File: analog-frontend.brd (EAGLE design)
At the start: 26.7 x 25.1 mm, 2 parts

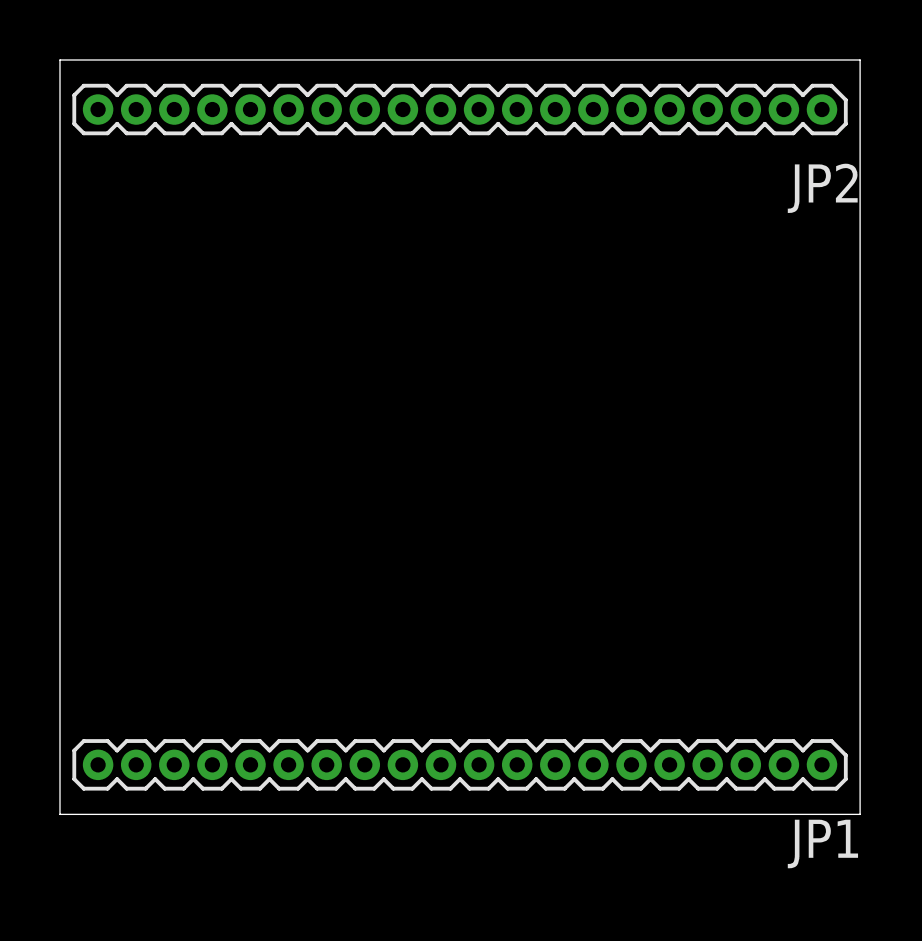
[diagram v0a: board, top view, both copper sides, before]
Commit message: added analog mux
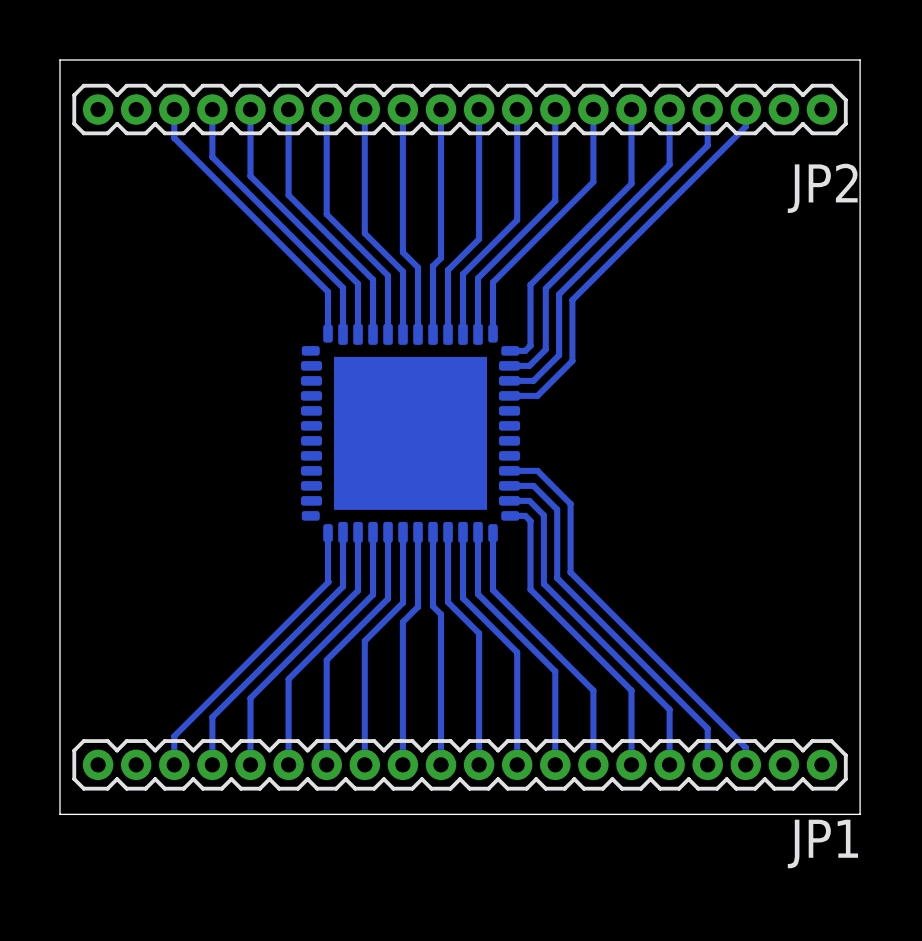
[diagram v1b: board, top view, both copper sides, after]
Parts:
- added IC1: ADG731, mor307:LFCSP48
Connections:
- new net N$1: IC1.12, JP1.18
- new net N$10: IC1.6, JP1.12
- new net N$11: IC1.5, JP1.11
- new net N$12: IC1.4, JP1.10
- new net N$13: IC1.3, JP1.9
- new net N$14: IC1.2, JP1.8
- new net N$15: IC1.1, JP1.7
- new net N$16: IC1.48, JP1.6
- new net N$17: IC1.47, JP1.5
- new net N$18: IC1.46, JP1.4
- new net N$19: IC1.26, JP2.17
- new net N$2: IC1.45, JP1.3
- new net N$20: IC1.27, JP2.16
- new net N$21: IC1.28, JP2.15
- new net N$22: IC1.29, JP2.14
- new net N$23: IC1.30, JP2.13
- new net N$24: IC1.31, JP2.12
- new net N$25: IC1.32, JP2.11
- new net N$26: IC1.33, JP2.10
- new net N$27: IC1.34, JP2.9
- new net N$28: IC1.35, JP2.8
- new net N$29: IC1.36, JP2.7
- new net N$3: IC1.25, JP2.18
- new net N$30: IC1.37, JP2.6
- new net N$31: IC1.38, JP2.5
- new net N$32: IC1.39, JP2.4
- new net N$4: IC1.40, JP2.3
- new net N$5: IC1.11, JP1.17
- new net N$6: IC1.10, JP1.16
- new net N$7: IC1.9, JP1.15
- new net N$8: IC1.8, JP1.14
- new net N$9: IC1.7, JP1.13
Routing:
- net N$2: track 0.00 -> 13.6 mm
- net N$4: track 0.00 -> 13.4 mm
- net N$18: track 0.00 -> 12.5 mm
- net N$32: track 0.00 -> 12.2 mm
- net N$17: track 0.00 -> 11.4 mm
- net N$31: track 0.00 -> 11.1 mm
- net N$16: track 0.00 -> 10.3 mm
- net N$30: track 0.00 -> 10.0 mm
- net N$1: track 0.00 -> 9.86 mm
- net N$3: track 0.00 -> 9.59 mm
- net N$5: track 0.00 -> 9.55 mm
- net N$19: track 0.00 -> 9.30 mm
- net N$6: track 0.00 -> 9.23 mm
- net N$15: track 0.00 -> 9.11 mm
- net N$20: track 0.00 -> 8.98 mm
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
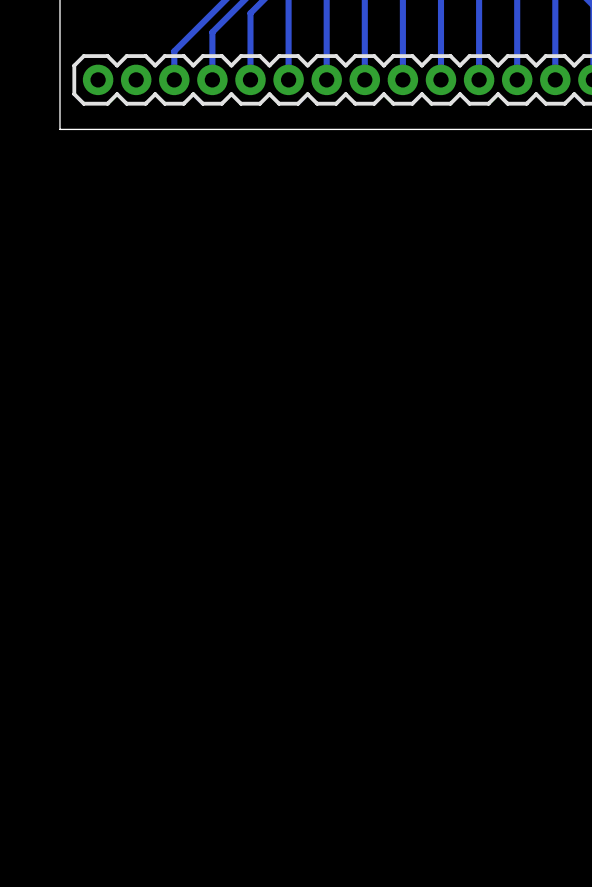
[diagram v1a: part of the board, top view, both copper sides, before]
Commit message: added power supply circuit
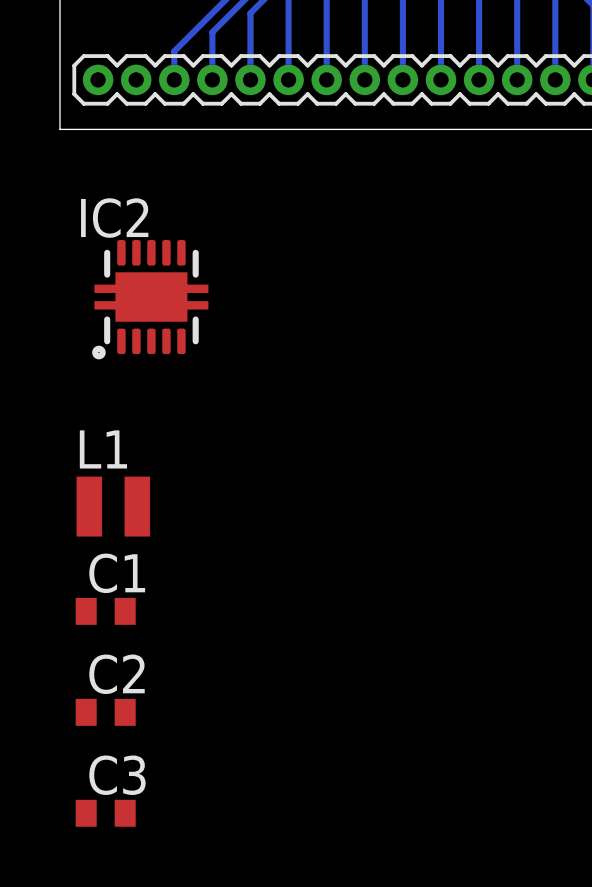
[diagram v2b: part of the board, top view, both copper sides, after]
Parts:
- added C1, C2, C3: (no value), rcl:C0402
- added IC2: TPS63031, mor307:S-PDSO-N10
- added L1: VLS25201, mor307:L1008
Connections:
- new net GND: C1.2, C2.2, C3.2, IC2.3, IC2.9
- new net N$33: IC2.4, L1.P$1
- new net N$34: IC2.2, L1.P$2
- new net N$35: C1.1, IC2.5, IC2.6, IC2.7, IC2.8
- new net N$37: C2.1, C3.1, IC2.1, IC2.10
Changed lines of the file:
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@@
 <element name="JP2" library="mor307" package="1X20" value="M20" x="25.4" y="23.495" rot="R180"/>
 <element name="IC1" library="mor307" package="LFCSP48" value="ADG731" x="11.684" y="12.7" rot="MR90"/>
+<element name="IC2" library="mor307" package="S-PDSO-N10" value="TPS63031" x="3.048" y="-5.588"/>
+<element name="L1" library="mor307" package="L1008" value="VLS25201" x="1.778" y="-12.573"/>
+<element name="C1" library="rcl" package="C0402" value="" x="1.524" y="-16.0655"/>
+<element name="C2" library="rcl" package="C0402" value="" x="1.524" y="-19.431"/>
+<element name="C3" library="rcl" package="C0402" value="" x="1.524" y="-22.7965"/>
 </elements>
 <signals>
@@
 <wire x1="16.637" y1="17.3355" x2="16.637" y2="15.3035" width="0.2032" layer="16"/>
 </signal>
+<signal name="GND">
+<contactref element="C1" pad="2"/>
+<contactref element="C2" pad="2"/>
+<contactref element="IC2" pad="3"/>
+<contactref element="IC2" pad="9"/>
+<contactref element="C3" pad="2"/>
+<wire x1="2.174" y1="-19.431" x2="2.174" y2="-22.7965" width="0" layer="19" extent="1-1"/>
+<wire x1="2.174" y1="-16.0655" x2="2.174" y2="-19.431" width="0" layer="19" extent="1-1"/>
+<wire x1="3.048" y1="-7.063" x2="2.174" y2="-16.0655" width="0" layer="19" extent="1-1"/>
+<wire x1="2.548" y1="-4.113" x2="3.048" y2="-7.063" width="0" layer="19" extent="1-1"/>
+</signal>
+<signal name="N$33">
+<contactref element="IC2" pad="4"/>
+<contactref element="L1" pad="P$1"/>
+<wire x1="3.548" y1="-7.063" x2="0.978" y2="-12.573" width="0" layer="19" extent="1-1"/>
+</signal>
+<signal name="N$34">
+<contactref element="L1" pad="P$2"/>
+<contactref element="IC2" pad="2"/>
+<wire x1="2.548" y1="-7.063" x2="2.578" y2="-12.573" width="0" layer="19" extent="1-1"/>
+</signal>
+<signal name="N$35">
+<contactref element="IC2" pad="7"/>
+<contactref element="IC2" pad="5"/>
+<contactref element="IC2" pad="8"/>
+<contactref element="IC2" pad="6"/>
+<contactref element="C1" pad="1"/>
+<wire x1="4.048" y1="-7.063" x2="0.874" y2="-16.0655" width="0" layer="19" extent="1-1"/>
+<wire x1="4.048" y1="-4.113" x2="4.048" y2="-7.063" width="0" layer="19" extent="1-1"/>
+<wire x1="3.548" y1="-4.113" x2="4.048" y2="-4.113" width="0" layer="19" extent="1-1"/>
+<wire x1="3.048" y1="-4.113" x2="3.548" y2="-4.113" width="0" layer="19" extent="1-1"/>
+</signal>
+<signal name="N$37">
+<contactref element="IC2" pad="1"/>
+<contactref element="C2" pad="1"/>
+<contactref element="IC2" pad="10"/>
+<contactref element="C3" pad="1"/>
+<wire x1="0.874" y1="-19.431" x2="0.874" y2="-22.7965" width="0" layer="19" extent="1-1"/>
+<wire x1="2.048" y1="-7.063" x2="0.874" y2="-19.431" width="0" layer="19" extent="1-1"/>
+<wire x1="2.048" y1="-4.113" x2="2.048" y2="-7.063" width="0" layer="19" extent="1-1"/>
+</signal>
 </signals>

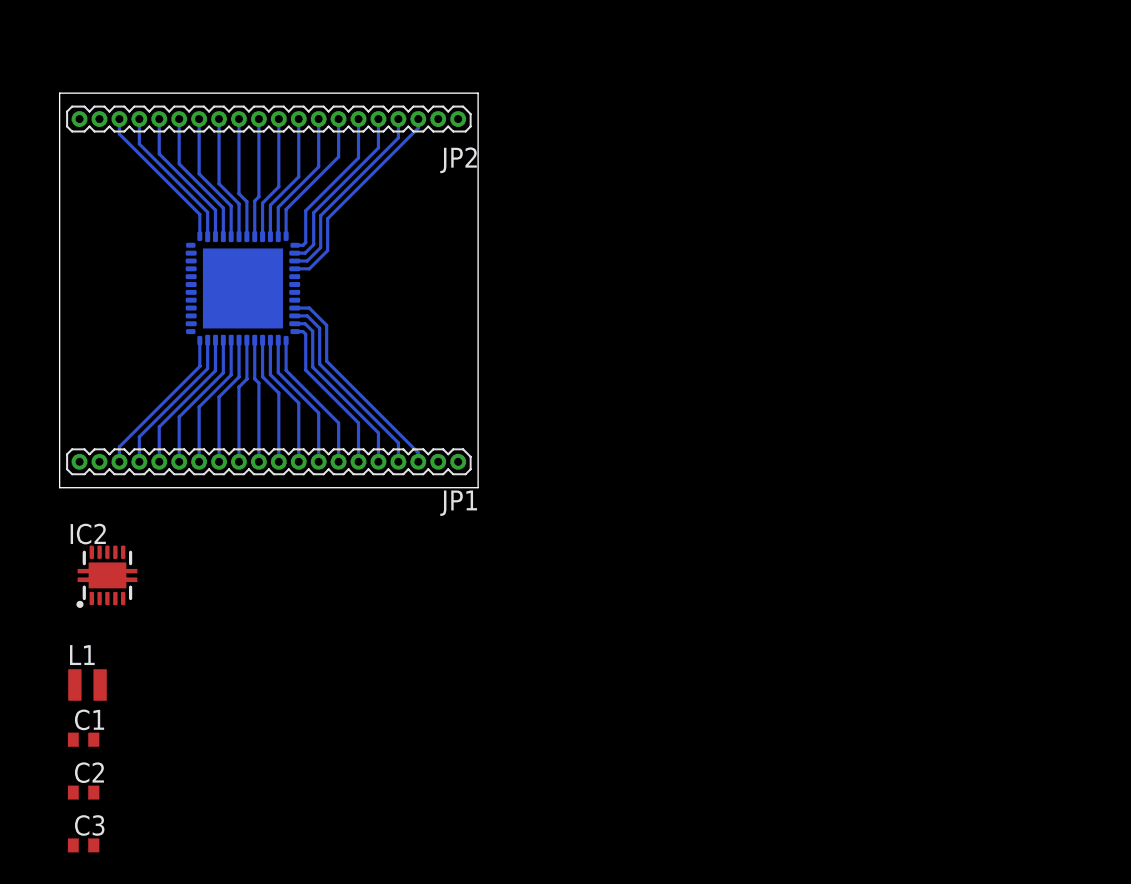
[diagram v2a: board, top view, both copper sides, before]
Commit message: added mcu, radio and finished analog frontend
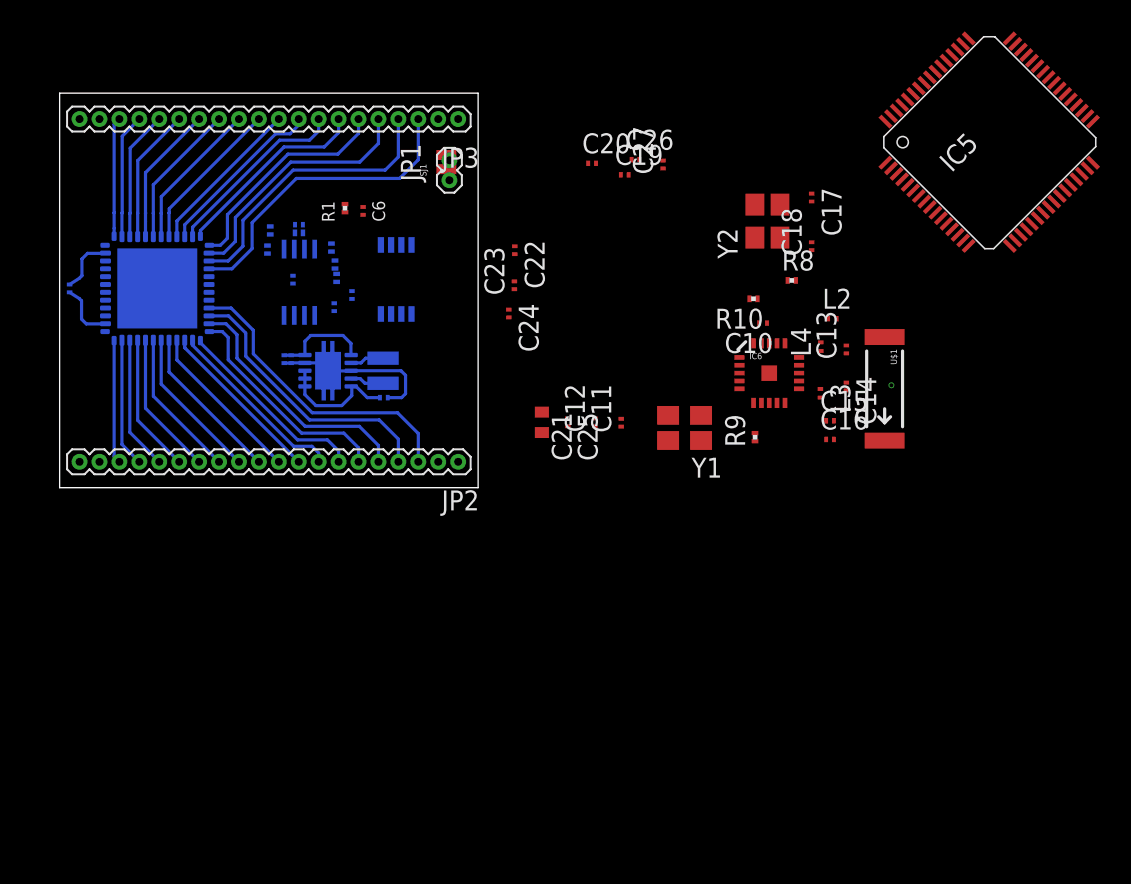
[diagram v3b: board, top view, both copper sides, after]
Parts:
- added C10, C11, C12, C13, C14, C15, C16, C17, C18, C19, C20, C22, C23, C24, C25, C26, C27, C4, C5, C6, C7, C8, C9: (no value), rcl:C0201
- added C21: (no value), rcl:C0402
- added IC3: INA332, mor307:DGK_S-PDSO-G8
- added IC4: OPA2320, mor307:MSOP08
- added IC5: TM4C123G, mor307:LQFP64
- added IC6: NRF24L01SMD, SparkFun-RF:QFN20
- added JP3: M20, mor307:1X20
- added L2, L3, L4: (no value), rcl:L0201
- added R1, R10, R2, R3, R4, R5, R6, R7, R8, R9: (no value), rcl:R0201
- added SJ1: (no value), SparkFun-Passives:PAD-JUMPER-2-NO_NO_SILK
- added U$1: ANTENNA2SMD5, SparkFun-RF:ANTENNA-CHIP5
- added Y1, Y2: CRYSTAL3X2, mor307:SMDCRYSTAL3X2
- C1, C2, C3: device rcl:C0402 -> rcl:C0201
- JP1: value M20 -> M02; device mor307:1X20 -> mor307:1X02
- moved C3 35.5 mm to (0.64, 12.7), flipped to the bottom, turned to 90 degrees
- moved C2 30.6 mm to (14.8, 8.19), flipped to the bottom, turned to 270 degrees
- moved C1 29.0 mm to (20.7, 5.74), flipped to the bottom, turned to 180 degrees
- moved L1 27.5 mm to (20.6, 7.45), flipped to the bottom, turned to 90 degrees
- moved JP2 21.8 mm to (25.4, 1.65)
- moved JP1 19.2 mm to (24.8, 20.9), turned to 90 degrees
- moved IC2 19.2 mm to (17.1, 7.45), flipped to the bottom, turned to 270 degrees
- moved IC1 5.46 mm to (6.22, 12.7)
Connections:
- new net +3V3: C2.1, C22.1, C23.1, C24.1, C25.1, C26.1, C27.1, C4.1, IC2.1, IC2.10, IC5.11, IC5.2, IC5.26, IC5.37, IC5.42, IC5.54, IC6.15, IC6.18, IC6.7, R10.1
- new net GNDA: C3.2, C5.1, C8.1, IC1.23, IC1.24, IC3.4, IC4.4, JP1.2, JP3.2, R5.1, SJ1.1
- new net N$36: C7.1, IC3.5, IC4.1, R2.2
- new net N$38: C6.1, IC3.1, R1.1, R2.1
- new net N$39: C9.2, IC4.6, R4.2, R6.1
- new net N$40: C17.1, IC5.41, Y2.3
- new net N$41: C9.1, IC4.7, R4.1
- new net N$42: C7.2, IC4.2, R3.2
- new net N$43: C10.2, IC6.19
- new net N$44: IC6.16, R8.2
- new net N$45: C19.1, C20.1, C21.1, IC5.25, IC5.56
- new net N$46: C11.1, IC6.9, R9.2, Y1.1
- new net N$47: IC4.5, R5.2, R7.2
- new net N$48: C12.1, IC6.10, R9.1, Y1.3
- new net N$49: IC5.38, R10.2
- new net N$50: IC6.12, L3.1, L4.1
- new net N$51: IC6.13, L2.1, L4.2
- new net N$52: C15.1, C16.1, IC6.11, L3.2
- new net N$53: C13.2, L2.2
- new net N$54: C13.1, C14.1, U$1.FEED
- new net RXD: IC5.18
- new net TCK: IC5.52
- new net TDI: IC5.50
- new net TDO: IC5.49
- new net TMS: IC5.51
- new net TXD: IC5.17
- new net VCM: IC4.3
- new net VDDA: C1.1, C3.1, C5.2, C8.2, IC1.13, IC1.14, IC2.5, IC2.6, IC2.7, IC2.8, IC3.7, IC3.8, IC4.8, JP1.1, R7.1
- new net VOUT: C6.2, IC3.6, R1.2, R3.1, R6.2
- net GND: now also C10.1, C11.2, C12.2, C14.2, C15.2, C16.2, C17.2, C18.2, C19.2, C20.2, C21.2, C22.2, C23.2, C24.2, C25.2, C26.2, C27.2, C4.2, IC5.12, IC5.27, IC5.3, IC5.32, IC5.34, IC5.35, IC5.39, IC5.55, IC6.0, IC6.14, IC6.17, IC6.20, IC6.8, R8.1, SJ1.2; no longer C3.2
- net N$1: now also JP2.18; no longer JP1.18
- net N$10: now also JP2.12; no longer JP1.12
- net N$11: now also JP2.11; no longer JP1.11
- net N$12: now also JP2.10; no longer JP1.10
- net N$13: now also JP2.9; no longer JP1.9
- net N$14: now also JP2.8; no longer JP1.8
- net N$15: now also JP2.7; no longer JP1.7
- net N$16: now also JP2.6; no longer JP1.6
- net N$17: now also JP2.5; no longer JP1.5
- net N$18: now also JP2.4; no longer JP1.4
- net N$19: now also JP3.17; no longer JP2.17
- net N$2: now also JP2.3; no longer JP1.3
- net N$20: now also JP3.16; no longer JP2.16
- net N$21: now also JP3.15; no longer JP2.15
- net N$22: now also JP3.14; no longer JP2.14
- net N$23: now also JP3.13; no longer JP2.13
- net N$24: now also JP3.12; no longer JP2.12
- net N$25: now also JP3.11; no longer JP2.11
- net N$26: now also JP3.10; no longer JP2.10
- net N$27: now also JP3.9; no longer JP2.9
- net N$28: now also JP3.8; no longer JP2.8
- net N$29: now also JP3.7; no longer JP2.7
- net N$3: now also JP3.18; no longer JP2.18
- net N$30: now also JP3.6; no longer JP2.6
- net N$31: now also JP3.5; no longer JP2.5
- net N$32: now also JP3.4; no longer JP2.4
- net N$35: now also IC1.43, IC3.3; no longer C1.1, IC2.5, IC2.6, IC2.7, IC2.8
- net N$37: now also C18.1, IC5.40, Y2.1; no longer C2.1, C3.1, IC2.1, IC2.10
- net N$4: now also JP3.3; no longer JP2.3
- net N$5: now also JP2.17; no longer JP1.17
- net N$6: now also JP2.16; no longer JP1.16
- net N$7: now also JP2.15; no longer JP1.15
- net N$8: now also JP2.14; no longer JP1.14
- net N$9: now also JP2.13; no longer JP1.13
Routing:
- net VDDA: track 0.00 -> 11.6 mm
- net GND: track 0.00 -> 10.5 mm, vias 0 -> 1
- net N$4: track 13.4 -> 19.8 mm
- net +3V3: track 0.00 -> 6.25 mm
- net N$32: track 12.2 -> 18.2 mm
- net N$2: track 13.6 -> 19.3 mm
- net N$18: track 12.5 -> 17.6 mm
- net N$31: track 11.1 -> 16.1 mm
- net N$17: track 11.4 -> 15.9 mm
- net N$30: track 10.0 -> 14.2 mm
- net N$16: track 10.3 -> 14.3 mm
- net N$29: track 8.86 -> 12.6 mm
- net GNDA: track 0.00 -> 3.69 mm
- net N$28: track 8.56 -> 11.9 mm
- net N$15: track 9.11 -> 12.5 mm
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
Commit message: routing complete!
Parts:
- removed SJ1: (no value), SparkFun-Passives:PAD-JUMPER-2-NO_NO_SILK
- added C28: (no value), rcl:C0201
- added R11, R12, R13, R14: (no value), rcl:R0201
- added TP1, TP2, TP3, TP4, TP5, TP6, TP7, TP8, TP9: PTR1B1,27, testpad:B1,27
- moved IC5 51.7 mm to (8.15, 13.8), turned to 270 degrees
- moved C18 42.1 mm to (7.29, 4.52), turned to 270 degrees
- moved C17 38.9 mm to (11.7, 4.55)
- moved R10 37.8 mm to (6.71, 7.26), turned to 0 degrees
- moved Y2 37.5 mm to (9.45, 5.51), turned to 0 degrees
- moved C26 36.3 mm to (1.37, 12.8), turned to 270 degrees
- moved C20 34.1 mm to (0.79, 12.8), turned to 270 degrees
- moved C27 31.8 mm to (6.65, 20.8), turned to 180 degrees
- moved C14 30.8 mm to (22.2, 19.5), turned to 180 degrees
- moved C16 30.3 mm to (22.0, 16.5), turned to 270 degrees
- moved C15 29.3 mm to (22.5, 16.5), turned to 270 degrees
- moved C13 29.2 mm to (22.9, 19.2), turned to 270 degrees
- moved L3 28.9 mm to (21.9, 17.4)
- moved U$1 28.9 mm to (25.2, 15.4)
- moved IC6 28.2 mm to (19.4, 18.6)
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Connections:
- new net N$55: IC5.61, IC6.3
- new net N$56: IC5.62, IC6.2
- new net N$58: IC5.63, IC6.5
- new net N$59: IC5.1, IC6.1
- new net N$60: IC5.58, IC6.6
- new net N$61: IC5.64, IC6.4
- new net N$62: C28.1, IC3.2, R14.1
- new net PF1: IC1.18, IC5.29
- new net PF2: IC1.19, IC5.30
- new net PF3: IC1.17, IC5.31
- new net VCM1: IC4.3, JP2.1
- new net VCM2: JP2.20, R14.2
- new net VREF: C28.2, JP2.19
- net +3V3: now also TP8.TP
- net GND: now also R13.2, TP9.TP; no longer SJ1.2
- net GNDA: now also JP2.2, R12.2, R13.1; no longer JP3.2, SJ1.1
- net N$49: now also TP7.TP
- net RXD: now also TP1.TP
- net TCK: now also TP3.TP
- net TDI: now also TP5.TP
- net TDO: now also TP6.TP
- net TMS: now also TP4.TP
- net TXD: now also TP2.TP
- net VCM: now also JP3.1, R11.2, R12.1; no longer IC4.3
- net VDDA: now also R11.1
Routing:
- net GND: track 10.5 -> 116.3 mm, vias 1 -> 7
- net +3V3: track 6.25 -> 107.0 mm, vias 0 -> 5
- net GNDA: track 3.69 -> 87.5 mm, vias 0 -> 4
- net VDDA: track 11.6 -> 68.3 mm, vias 0 -> 5
- net N$62: track 0.00 -> 23.1 mm, vias 0 -> 2
- net VCM: track 0.00 -> 22.7 mm, vias 0 -> 1
- net N$45: track 0.00 -> 18.8 mm
- net VOUT: track 0.00 -> 18.4 mm
- net N$36: track 0.00 -> 14.0 mm, vias 0 -> 1
- net TDI: track 0.00 -> 13.2 mm
- net VCM1: track 0.00 -> 10.2 mm, vias 0 -> 3
- net TCK: track 0.00 -> 9.01 mm
- net N$42: track 0.00 -> 8.54 mm, vias 0 -> 1
- net TDO: track 0.00 -> 7.75 mm
- net N$48: track 0.00 -> 7.67 mm
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- added copper zone on layer 1, net GND
- added copper zone on layer 16, net GNDA
